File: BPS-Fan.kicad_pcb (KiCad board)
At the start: 2 copper layers, 57.3 x 75.4 mm, 37 parts, among them J1 LDRBRDConn, J10 FAN9, J11 FAN10, J12 FAN11, J13 FAN12, J2 FAN1, J3 FAN2, J4 FAN3, J5 FAN4, J6 FAN5, J7 FAN6, J8 FAN7, J9 FAN8, Q1 BUK9M23-80E, Q2 BUK9M23-80E, Q3 BUK9M23-80E, Q4 BUK9M23-80E

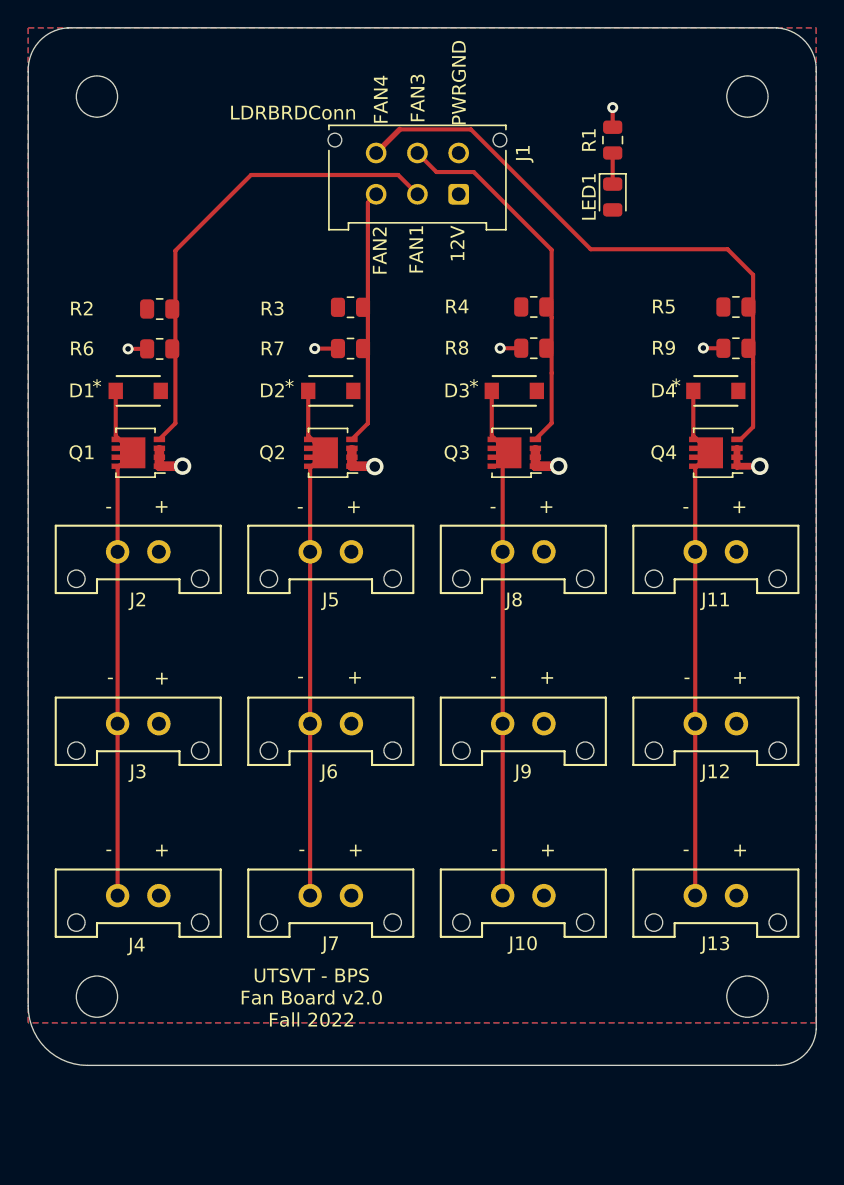
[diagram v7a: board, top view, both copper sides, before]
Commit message: added changes based on Hannah's comments
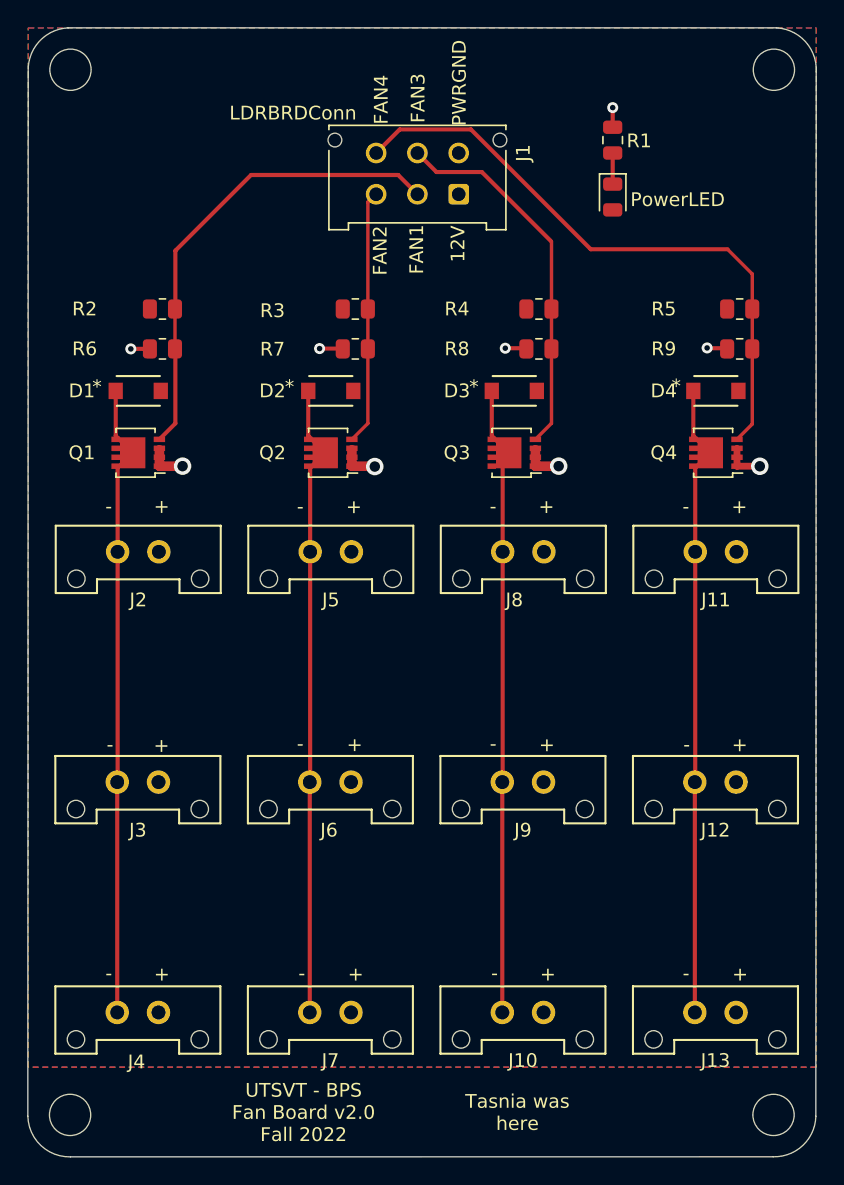
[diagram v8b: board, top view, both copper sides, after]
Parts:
- moved H4 8.82 mm to (131.5, 119.7)
- moved H2 8.81 mm to (182.7, 119.7)
- moved J10 8.49 mm to (166.0, 112.3)
- moved J13 8.49 mm to (180.0, 112.3)
- moved J4 8.49 mm to (138.0, 112.3)
- moved J7 8.49 mm to (152.0, 112.3)
- moved J12 4.24 mm to (180.0, 95.5)
- moved J3 4.24 mm to (138.0, 95.5)
- moved J6 4.24 mm to (152.0, 95.5)
- moved J9 4.24 mm to (166.0, 95.5)
- moved H1 2.74 mm to (131.6, 43.7)
- moved H3 2.74 mm to (182.7, 43.7)
- moved R4 0.40 mm to (165.6, 61.1)
- moved R8 0.38 mm to (165.6, 64.0)
- moved R3 0.37 mm to (152.3, 61.1)
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- renumbered LED1 to PowerLED
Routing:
- net Net-(D4-Pad2): track 37.7 -> 46.2 mm
- net Net-(D2-Pad2): track 37.7 -> 46.2 mm
- net Net-(D3-Pad2): track 37.4 -> 45.9 mm
- net Net-(D1-Pad2): track 37.9 -> 46.2 mm
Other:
- board size 57.3 x 75.4 mm -> 57.3 x 82.1 mm
- board text added: "Tasnia was here"
